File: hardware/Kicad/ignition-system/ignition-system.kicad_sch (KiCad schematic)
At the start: 29 parts, among them J1 Screw_Terminal_01x02, SW1 SW_Push, SW2 SW_SPDT

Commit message: fix: schematic wires & labels
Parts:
- removed R10: R, symbol Device:R
- renumbered Amarillo(Modo/Rol) to Amarillo(Modo/Rol)1, Azul(Sistema/Link) to Azul(Sistema/Link)1, CHRG to CHRG1, Display to Display1, InBatt to InBatt1, LORA to LORA2, ModuloDeCarga to ModuloDeCarga1, RaspberryPi_Pico to RaspberryPi_Pico1, Rojo(Armado/Peligro) to Rojo(Armado/Peligro)1, STDBY to STDBY1
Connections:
- net GND: now also Amarillo(Modo/Rol)1.1 (K), Azul(Sistema/Link)1.1 (K), Rojo(Armado/Peligro)1.1 (K), SW1.2
- net SCK: no longer Display1.2 (Pin_2), RaspberryPi_Pico1.7 (GPIO5)
- net VBUS: now also CHRG1.2 (A), STDBY1.2 (A)
- net VCC: no longer CHRG1.2 (A), STDBY1.2 (A)
- new net SCL: Display1.2 (Pin_2), RaspberryPi_Pico1.7 (GPIO5)

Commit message: feat: assign footprints
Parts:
- removed BT1: Battery_Cell, symbol Device:Battery_Cell
- AOD4184A1: footprint (none) -> Package_TO_SOT_SMD:TO-252-2
- C1, C2: footprint (none) -> Capacitor_SMD:C_0805_2012Metric
- Display1: footprint (none) -> Connector_PinHeader_2.54mm:PinHeader_1x04_P2.54mm_Vertical
- J1: footprint (none) -> TerminalBlock:TerminalBlock_MaiXu_MX126-5.0-02P_1x02_P5.00mm
- LORA1, LORA2: footprint (none) -> Connector_PinHeader_2.54mm:PinHeader_1x08_P2.54mm_Vertical
- R1, R11, R2, R3, R4, R5, R6, R7, R8, R9: footprint (none) -> Resistor_SMD:R_0805_2012Metric
- SW1, SW2: footprint (none) -> Connector_PinHeader_2.54mm:PinHeader_1x02_P2.54mm_Vertical
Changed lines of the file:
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@@
 	)
 	(junction
-		(at 73.66 58.42)
-		(diameter 0)
-		(color 0 0 0 0)
-	)
-	(junction
 		(at 52.07 74.93)
 		(diameter 0)
@@
 	)
 	(junction
-		(at 73.66 38.1)
-		(diameter 0)
-		(color 0 0 0 0)
-	)
-	(junction
 		(at 73.66 107.95)
 		(diameter 0)
@@
 	(wire
 		(pts
-			(xy 73.66 58.42) (xy 73.66 55.88)
-		)
-		(stroke
-			(width 0)
-			(type default)
-		)
-	)
-	(wire
-		(pts
 			(xy 243.84 66.04) (xy 246.38 66.04)
 		)
@@
 	(wire
 		(pts
-			(xy 73.66 38.1) (xy 73.66 48.26)
-		)
-		(stroke
-			(width 0)
-			(type default)
-		)
-	)
-	(wire
-		(pts
 			(xy 62.23 55.88) (xy 62.23 58.42)
 		)
@@
 			)
 		)
-		(property "Footprint" ""
+		(property "Footprint" "Resistor_SMD:R_0805_2012Metric"
 			(at 199.39 163.068 90)
 			(hide yes)
@@
 			)
 		)
-		(property "Footprint" ""
+		(property "Footprint" "Resistor_SMD:R_0805_2012Metric"
 			(at 199.39 137.668 90)
 			(hide yes)
@@
 			)
 		)
-		(property "Footprint" ""
+		(property "Footprint" "Resistor_SMD:R_0805_2012Metric"
 			(at 147.32 185.928 90)
 			(hide yes)
@@
 			)
 		)
-		(property "Footprint" ""
+		(property "Footprint" "TerminalBlock:TerminalBlock_MaiXu_MX126-5.0-02P_1x02_P5.00mm"
 			(at 67.31 167.64 0)
 			(hide yes)
@@
 			)
 		)
-		(property "Footprint" ""
+		(property "Footprint" "Capacitor_SMD:C_0805_2012Metric"
 			(at 74.6252 102.87 0)
 			(hide yes)
@@
 	)
 	(symbol
-		(lib_id "Device:Battery_Cell")
-		(at 73.66 53.34 0)
-		(unit 1)
-		(body_style 1)
-		(exclude_from_sim no)
-		(in_bom yes)
-		(on_board yes)
-		(in_pos_files yes)
-		(dnp no)
-		(fields_autoplaced yes)
-		(property "Reference" "BT1"
-			(at 77.47 50.2284 0)
-			(show_name no)
-			(do_not_autoplace no)
-			(effects
-				(font
-					(size 1.27 1.27)
-				)
-				(justify left)
-			)
-		)
-		(property "Value" "Battery_Cell"
-			(at 77.47 52.7684 0)
-			(show_name no)
-			(do_not_autoplace no)
-			(effects
-				(font
-					(size 1.27 1.27)
-				)
-				(justify left)
-			)
-		)
-		(property "Footprint" ""
-			(at 73.66 51.816 90)
-			(hide yes)
-			(show_name no)
-			(do_not_autoplace no)
-			(effects
-				(font
-					(size 1.27 1.27)
-				)
-			)
-		)
-		(property "Datasheet" ""
-			(at 73.66 51.816 90)
-			(hide yes)
-			(show_name no)
-			(do_not_autoplace no)
-			(effects
-				(font
-					(size 1.27 1.27)
-				)
-			)
-		)
-		(property "Description" "Single-cell battery"
-			(at 73.66 53.34 0)
-			(hide yes)
-			(show_name no)
-			(do_not_autoplace no)
-			(effects
-				(font
-					(size 1.27 1.27)
-				)
-			)
-		)
-		(property "Sim.Device" "V"
-			(at 73.66 53.34 0)
-			(hide yes)
-			(show_name no)
-			(do_not_autoplace no)
-			(effects
-				(font
-					(size 1.27 1.27)
-				)
-			)
-		)
-		(property "Sim.Type" "DC"
-			(at 73.66 53.34 0)
-			(hide yes)
-			(show_name no)
-			(do_not_autoplace no)
-			(effects
-				(font
-					(size 1.27 1.27)
-				)
-			)
-		)
-		(property "Sim.Pins" "1=+ 2=-"
-			(at 73.66 53.34 0)
-			(hide yes)
-			(show_name no)
-			(do_not_autoplace no)
-			(effects
-				(font
-					(size 1.27 1.27)
-				)
-			)
-		)
-		(pin "2"
-		)
-		(pin "1"
-		)
-		(instances
-			(project "ignition-system"
-				(path "/e17dc731-fbd5-49fb-b534-5ba28a19fa2e"
-					(reference "BT1")
-					(unit 1)
-				)
-			)
-		)
-	)
-	(symbol
 		(lib_id "Device:LED")
 		(at 156.21 184.15 0)
@@
 			)
 		)
-		(property "Footprint" ""
+		(property "Footprint" "Resistor_SMD:R_0805_2012Metric"
 			(at 60.452 44.45 90)
 			(hide yes)
@@
 			)
 		)
-		(property "Footprint" ""
+		(property "Footprint" "Connector_PinHeader_2.54mm:PinHeader_1x08_P2.54mm_Vertical"
 			(at 251.46 71.12 0)
 			(hide yes)
@@
 			)
 		)
-		(property "Footprint" ""
+		(property "Footprint" "Connector_PinHeader_2.54mm:PinHeader_1x02_P2.54mm_Vertical"
 			(at 45.72 162.56 0)
 			(hide yes)
@@
 			)
 		)
-		(property "Footprint" ""
+		(property "Footprint" "Capacitor_SMD:C_0805_2012Metric"
 			(at 25.0952 95.25 0)
 			(hide yes)
@@
 			)
 		)
-		(property "Footprint" ""
+		(property "Footprint" "Resistor_SMD:R_0805_2012Metric"
 			(at 44.45 179.578 90)
 			(hide yes)
@@
 			)
 		)
-		(property "Footprint" ""
+		(property "Footprint" "Resistor_SMD:R_0805_2012Metric"
 			(at 61.722 99.06 90)
 			(hide yes)
@@
 			)
 		)
-		(property "Footprint" ""
+		(property "Footprint" "Resistor_SMD:R_0805_2012Metric"
 			(at 60.452 52.07 90)
 			(hide yes)
@@
 			)
 		)
-		(property "Footprint" ""
+		(property "Footprint" "Connector_PinHeader_2.54mm:PinHeader_1x04_P2.54mm_Vertical"
 			(at 118.11 162.56 0)
 			(hide yes)
@@
 			)
 		)
-		(property "Footprint" ""
+		(property "Footprint" "Package_TO_SOT_SMD:TO-252-2"
 			(at 60.96 175.26 0)
 			(hide yes)
@@
 			)
 		)
-		(property "Footprint" ""
+		(property "Footprint" "Resistor_SMD:R_0805_2012Metric"
 			(at 199.39 150.368 90)
 			(hide yes)
@@
 			)
 		)
-		(property "Footprint" ""
+		(property "Footprint" "Connector_PinHeader_2.54mm:PinHeader_1x02_P2.54mm_Vertical"
 			(at 80.01 133.35 0)
 			(hide yes)
@@
 			)
 		)
-		(property "Footprint" ""
+		(property "Footprint" "Connector_PinHeader_2.54mm:PinHeader_1x08_P2.54mm_Vertical"
 			(at 217.17 71.12 0)
 			(hide yes)
@@
 			)
 		)
-		(property "Footprint" ""
+		(property "Footprint" "Resistor_SMD:R_0805_2012Metric"
 			(at 47.752 184.15 90)
 			(hide yes)
@@
 			)
 		)
-		(property "Footprint" ""
+		(property "Footprint" "Resistor_SMD:R_0805_2012Metric"
 			(at 147.32 173.228 90)
 			(hide yes)

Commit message: feat: add components on pcb editor
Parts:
- SW2: footprint Connector_PinHeader_2.54mm:PinHeader_1x02_P2.54mm_Vertical -> Connector_PinHeader_2.54mm:PinHeader_1x03_P2.54mm_Vertical
- renumbered Azul(Sistema/Link)1 to BLED1, Rojo(Armado/Peligro)1 to RLED1, Amarillo(Modo/Rol)1 to YLED1
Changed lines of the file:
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@@
 			)
 		)
-		(property "Footprint" "Connector_PinHeader_2.54mm:PinHeader_1x02_P2.54mm_Vertical"
+		(property "Footprint" "Connector_PinHeader_2.54mm:PinHeader_1x03_P2.54mm_Vertical"
 			(at 45.72 162.56 0)
 			(hide yes)
@@
 		(dnp no)
 		(fields_autoplaced yes)
-		(property "Reference" "Rojo(Armado/Peligro)1"
+		(property "Reference" "RLED1"
 			(at 187.6425 154.94 0)
 			(show_name no)
@@
 			(project "ignition-system"
 				(path "/e17dc731-fbd5-49fb-b534-5ba28a19fa2e"
-					(reference "Rojo(Armado/Peligro)1")
+					(reference "RLED1")
 					(unit 1)
 				)
@@
 		(dnp no)
 		(fields_autoplaced yes)
-		(property "Reference" "Amarillo(Modo/Rol)1"
+		(property "Reference" "YLED1"
 			(at 187.6425 142.24 0)
 			(show_name no)
@@
 			(project "ignition-system"
 				(path "/e17dc731-fbd5-49fb-b534-5ba28a19fa2e"
-					(reference "Amarillo(Modo/Rol)1")
+					(reference "YLED1")
 					(unit 1)
 				)
@@
 		(dnp no)
 		(fields_autoplaced yes)
-		(property "Reference" "Azul(Sistema/Link)1"
+		(property "Reference" "BLED1"
 			(at 187.6425 129.54 0)
 			(show_name no)
@@
 			(project "ignition-system"
 				(path "/e17dc731-fbd5-49fb-b534-5ba28a19fa2e"
-					(reference "Azul(Sistema/Link)1")
-					(unit 1)
-				)
+					(reference "BLED1")
+					(unit 1)
+				)

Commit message: fix: wire TP4056 CE to VBUS, TEMP to GND, drop DIO labels
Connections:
- net VCC is gone; now on net VBUS: ModuloDeCarga1.8 (CE)
- net GND: now also ModuloDeCarga1.1 (TEMP)
- no-connect marks 32 -> 24

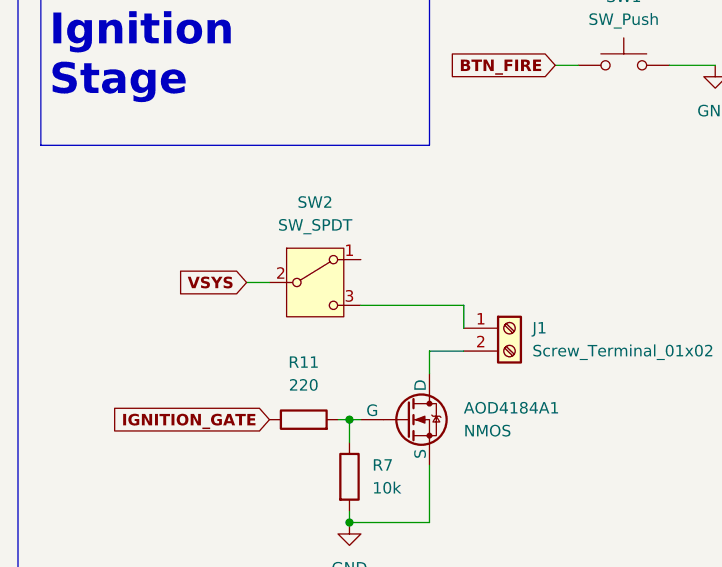
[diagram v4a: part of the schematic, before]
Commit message: fix: wire SW2 common to ignitor, throws to VSYS and GND
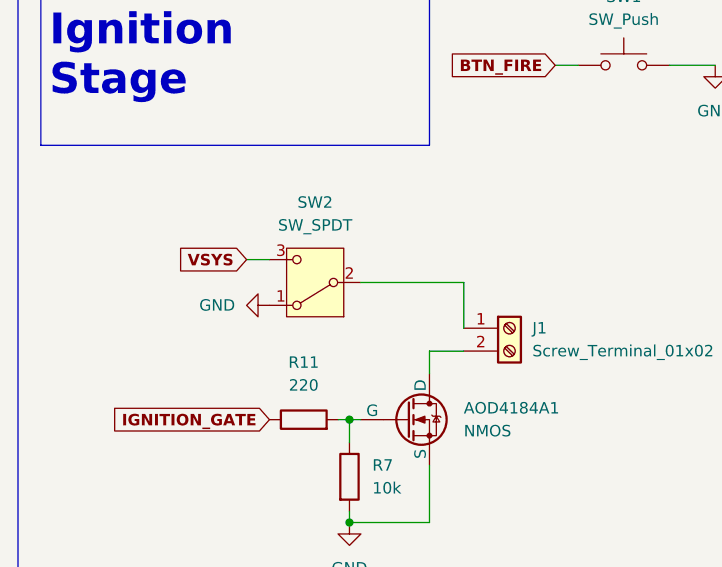
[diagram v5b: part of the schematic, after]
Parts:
- SW2: footprint Connector_PinHeader_2.54mm:PinHeader_1x03_P2.54mm_Vertical -> Button_Switch_THT:SW_E-Switch_EG1224_SPDT_Angled
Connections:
- net GND: now also SW2.1 (A)
- net VSYS: now also SW2.3 (C); no longer SW2.2 (B)
- net at J1.1 (Pin_1): now also SW2.2 (B); no longer SW2.3 (C)
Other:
- moved on the sheet: SW2
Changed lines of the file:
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@@
 	(wire
 		(pts
-			(xy 38.1 162.56) (xy 40.64 162.56)
+			(xy 38.1 160.02) (xy 40.64 160.02)
 		)
 		(stroke
@@
 	(wire
 		(pts
+			(xy 62.23 167.64) (xy 62.23 162.56)
+		)
+		(stroke
+			(width 0)
+			(type default)
+		)
+	)
+	(wire
+		(pts
 			(xy 203.2 161.29) (xy 207.01 161.29)
 		)
@@
 	(wire
 		(pts
-			(xy 50.8 165.1) (xy 62.23 165.1)
-		)
-		(stroke
-			(width 0)
-			(type default)
-		)
-	)
-	(wire
-		(pts
 			(xy 193.04 148.59) (xy 195.58 148.59)
 		)
@@
 	(wire
 		(pts
-			(xy 62.23 165.1) (xy 62.23 167.64)
-		)
-		(stroke
-			(width 0)
-			(type default)
-		)
-	)
-	(wire
-		(pts
 			(xy 193.04 161.29) (xy 195.58 161.29)
 		)
@@
 	(wire
 		(pts
+			(xy 62.23 162.56) (xy 50.8 162.56)
+		)
+		(stroke
+			(width 0)
+			(type default)
+		)
+	)
+	(wire
+		(pts
 			(xy 203.2 148.59) (xy 207.01 148.59)
 		)
@@
 	(global_label "VSYS"
 		(shape input)
-		(at 38.1 162.56 180)
+		(at 38.1 160.02 180)
 		(fields_autoplaced yes)
 		(effects
@@
 		)
 		(property "Intersheetrefs" "${INTERSHEET_REFS}"
-			(at 30.0426 162.56 0)
+			(at 30.0426 160.02 0)
 			(hide yes)
 			(show_name no)
@@
 				)
 				(justify left)
+			)
+		)
+	)
+	(symbol
+		(lib_id "power:GND")
+		(at 40.64 165.1 270)
+		(unit 1)
+		(body_style 1)
+		(exclude_from_sim no)
+		(in_bom yes)
+		(on_board yes)
+		(in_pos_files yes)
+		(dnp no)
+		(fields_autoplaced yes)
+		(property "Reference" "#PWR015"
+			(at 34.29 165.1 0)
+			(hide yes)
+			(show_name no)
+			(do_not_autoplace no)
+			(effects
+				(font
+					(size 1.27 1.27)
+				)
+			)
+		)
+		(property "Value" "GND"
+			(at 36.83 165.0999 90)
+			(show_name no)
+			(do_not_autoplace no)
+			(effects
+				(font
+					(size 1.27 1.27)
+				)
+				(justify right)
+			)
+		)
+		(property "Footprint" ""
+			(at 40.64 165.1 0)
+			(hide yes)
+			(show_name no)
+			(do_not_autoplace no)
+			(effects
+				(font
+					(size 1.27 1.27)
+				)
+			)
+		)
+		(property "Datasheet" ""
+			(at 40.64 165.1 0)
+			(hide yes)
+			(show_name no)
+			(do_not_autoplace no)
+			(effects
+				(font
+					(size 1.27 1.27)
+				)
+			)
+		)
+		(property "Description" "Power symbol creates a global label with name \"GND\" , ground"
+			(at 40.64 165.1 0)
+			(hide yes)
+			(show_name no)
+			(do_not_autoplace no)
+			(effects
+				(font
+					(size 1.27 1.27)
+				)
+			)
+		)
+		(pin "1"
+		)
+		(instances
+			(project "ignition-system"
+				(path "/e17dc731-fbd5-49fb-b534-5ba28a19fa2e"
+					(reference "#PWR015")
+					(unit 1)
+				)
 			)
 		)
@@
 	(symbol
 		(lib_id "Switch:SW_SPDT")
-		(at 45.72 162.56 0)
+		(at 45.72 162.56 180)
 		(unit 1)
 		(body_style 1)
@@
 			)
 		)
-		(property "Footprint" "Connector_PinHeader_2.54mm:PinHeader_1x03_P2.54mm_Vertical"
+		(property "Footprint" "Button_Switch_THT:SW_E-Switch_EG1224_SPDT_Angled"
 			(at 45.72 162.56 0)
 			(hide yes)
@@
 		)
 		(property "Datasheet" ""
-			(at 45.72 170.18 0)
-			(hide yes)
-			(show_name no)
+			(at 45.72 154.94 0)
+			(hide yes)
+			(show_name no)

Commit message: chore(update): bump inputs
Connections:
- net GND: now also SW2.3 (C); no longer SW2.1 (A)
- net VSYS: now also SW2.1 (A); no longer SW2.3 (C)

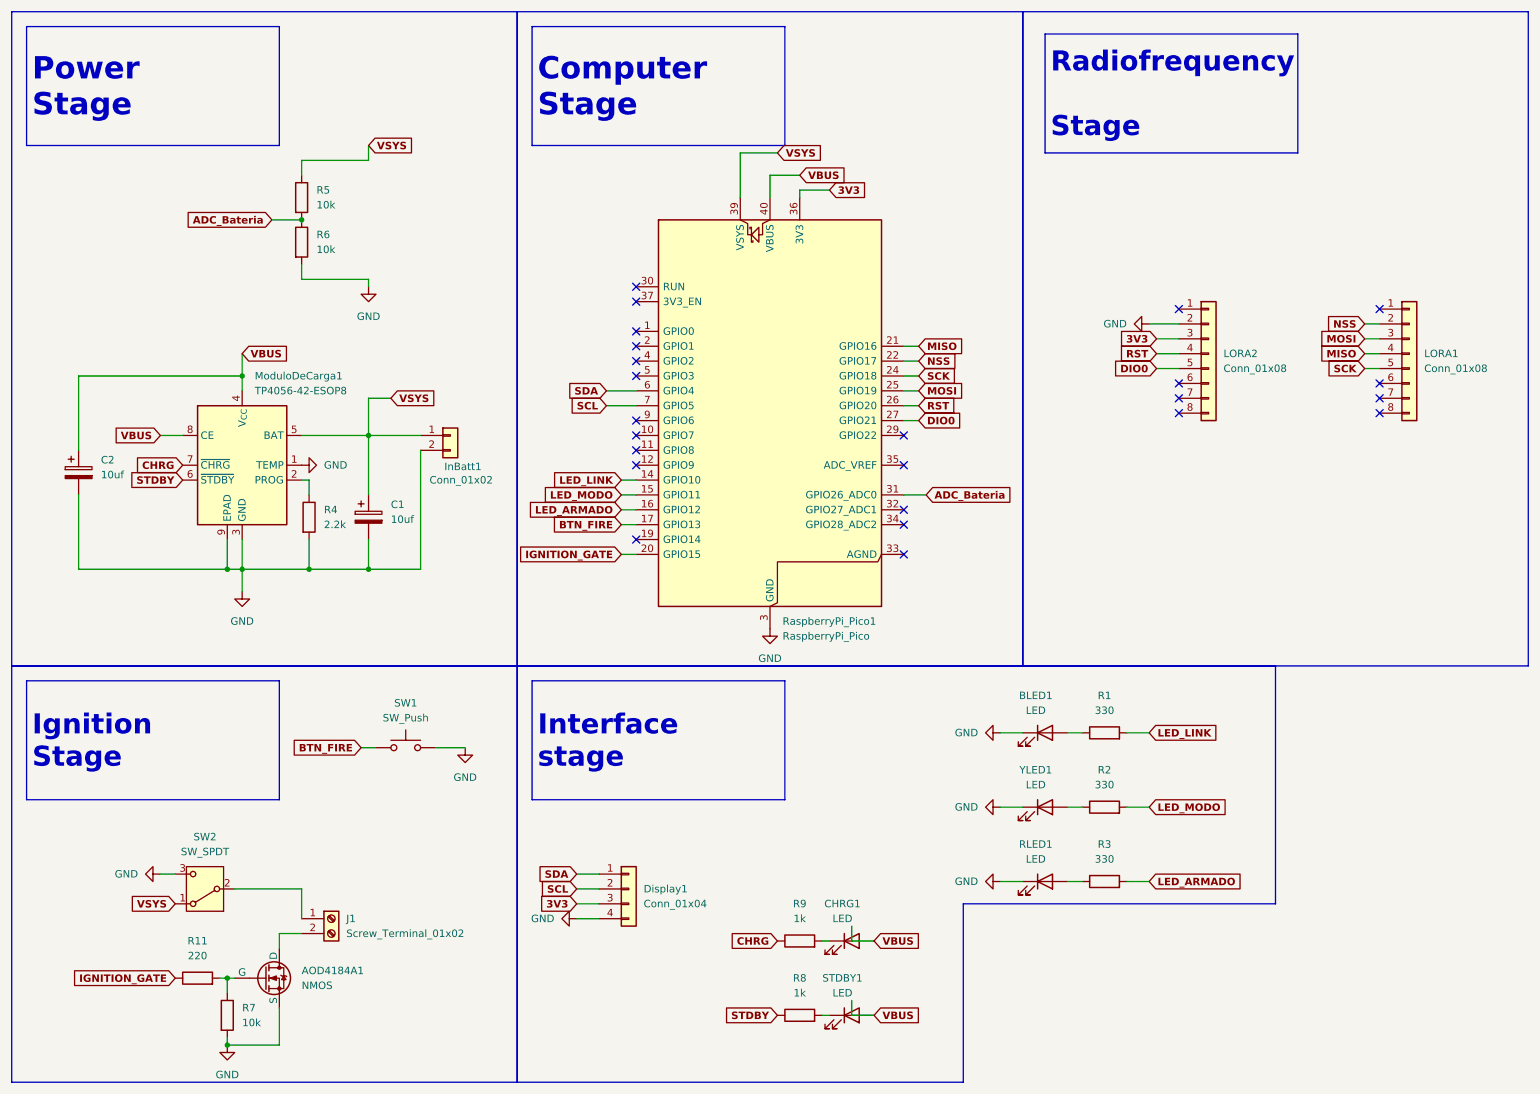
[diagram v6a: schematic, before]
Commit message: chore(kicad): renombrar designators con chip en ignition-system
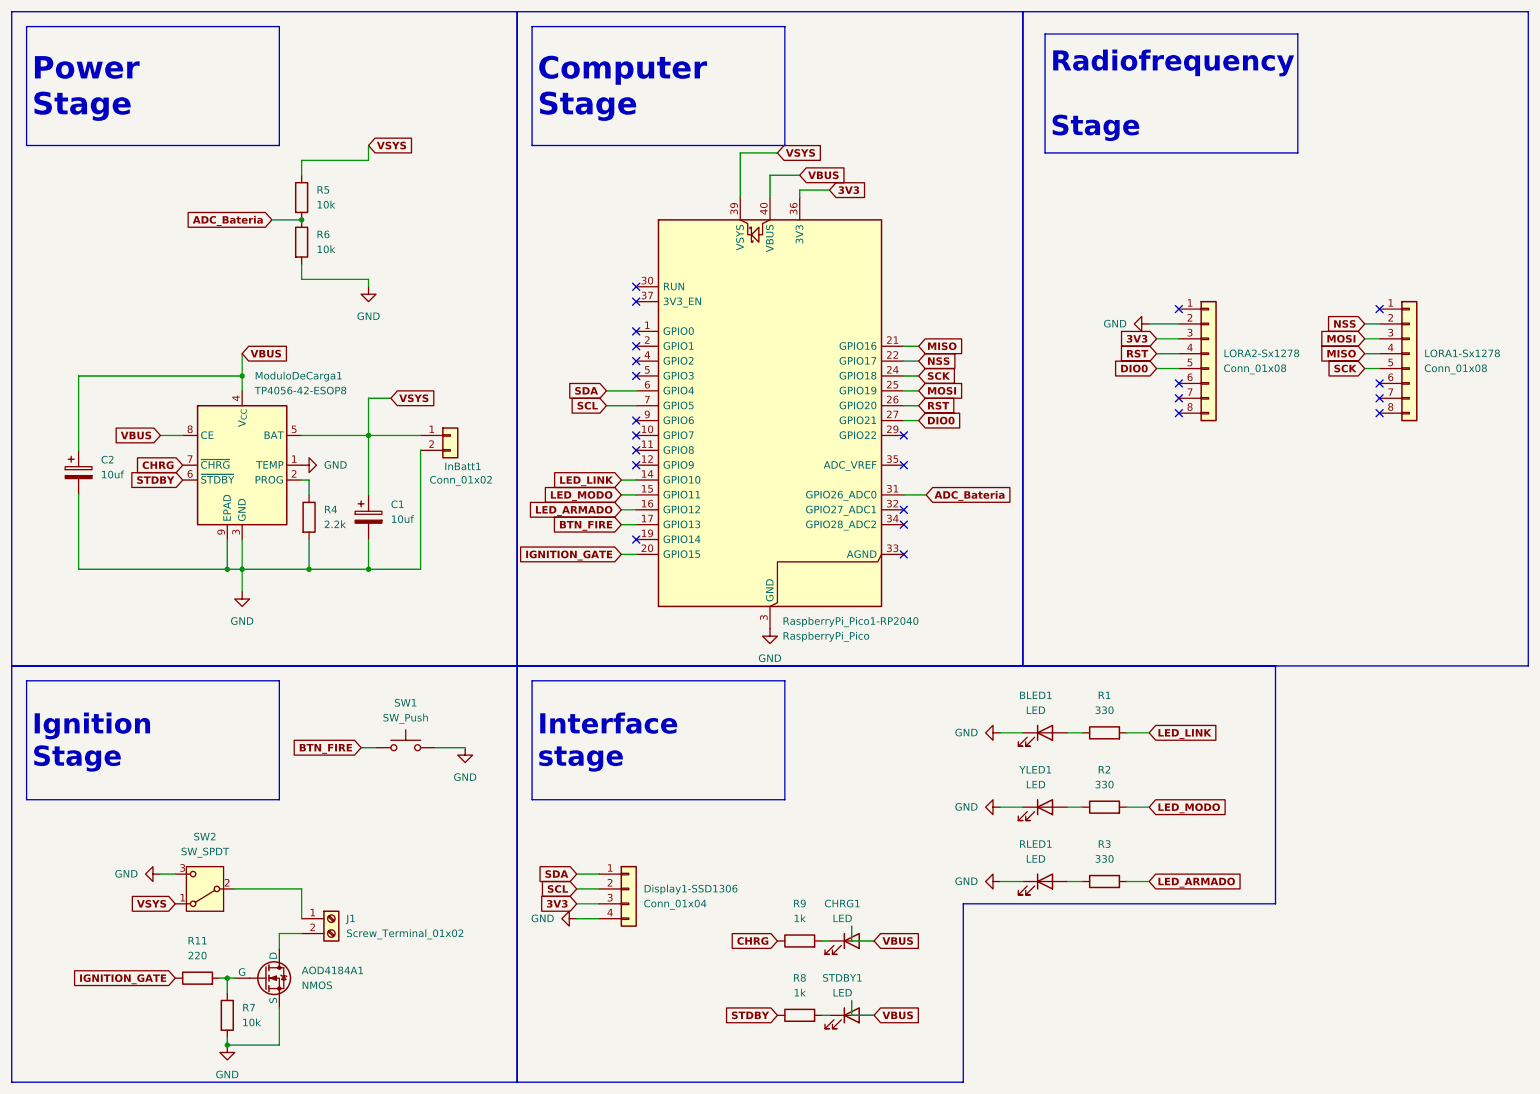
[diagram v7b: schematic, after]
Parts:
- renumbered Display1 to Display1-SSD1306, LORA1 to LORA1-Sx1278, LORA2 to LORA2-Sx1278, RaspberryPi_Pico1 to RaspberryPi_Pico1-RP2040
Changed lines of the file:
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@@
 		(dnp no)
 		(fields_autoplaced yes)
-		(property "Reference" "LORA1"
+		(property "Reference" "LORA1-Sx1278"
 			(at 254 71.1199 0)
 			(show_name no)
@@
 			(project "ignition-system"
 				(path "/e17dc731-fbd5-49fb-b534-5ba28a19fa2e"
-					(reference "LORA1")
+					(reference "LORA1-Sx1278")
 					(unit 1)
 				)
@@
 		(dnp no)
 		(fields_autoplaced yes)
-		(property "Reference" "RaspberryPi_Pico1"
+		(property "Reference" "RaspberryPi_Pico1-RP2040"
 			(at 144.3833 116.84 0)
 			(show_name no)
@@
 			(project "ignition-system"
 				(path "/e17dc731-fbd5-49fb-b534-5ba28a19fa2e"
-					(reference "RaspberryPi_Pico1")
+					(reference "RaspberryPi_Pico1-RP2040")
 					(unit 1)
 				)
@@
 		(dnp no)
 		(fields_autoplaced yes)
-		(property "Reference" "Display1"
+		(property "Reference" "Display1-SSD1306"
 			(at 120.65 162.5599 0)
 			(show_name no)
@@
 			(project "ignition-system"
 				(path "/e17dc731-fbd5-49fb-b534-5ba28a19fa2e"
-					(reference "Display1")
+					(reference "Display1-SSD1306")
 					(unit 1)
 				)
@@
 		(dnp no)
 		(fields_autoplaced yes)
-		(property "Reference" "LORA2"
+		(property "Reference" "LORA2-Sx1278"
 			(at 219.71 71.1199 0)
 			(show_name no)
@@
 			(project "ignition-system"
 				(path "/e17dc731-fbd5-49fb-b534-5ba28a19fa2e"
-					(reference "LORA2")
-					(unit 1)
-				)
+					(reference "LORA2-Sx1278")
+					(unit 1)
+				)
